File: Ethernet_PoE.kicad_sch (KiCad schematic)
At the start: 7 parts, among them J201 7499511002A, U201 AG5712-LPB

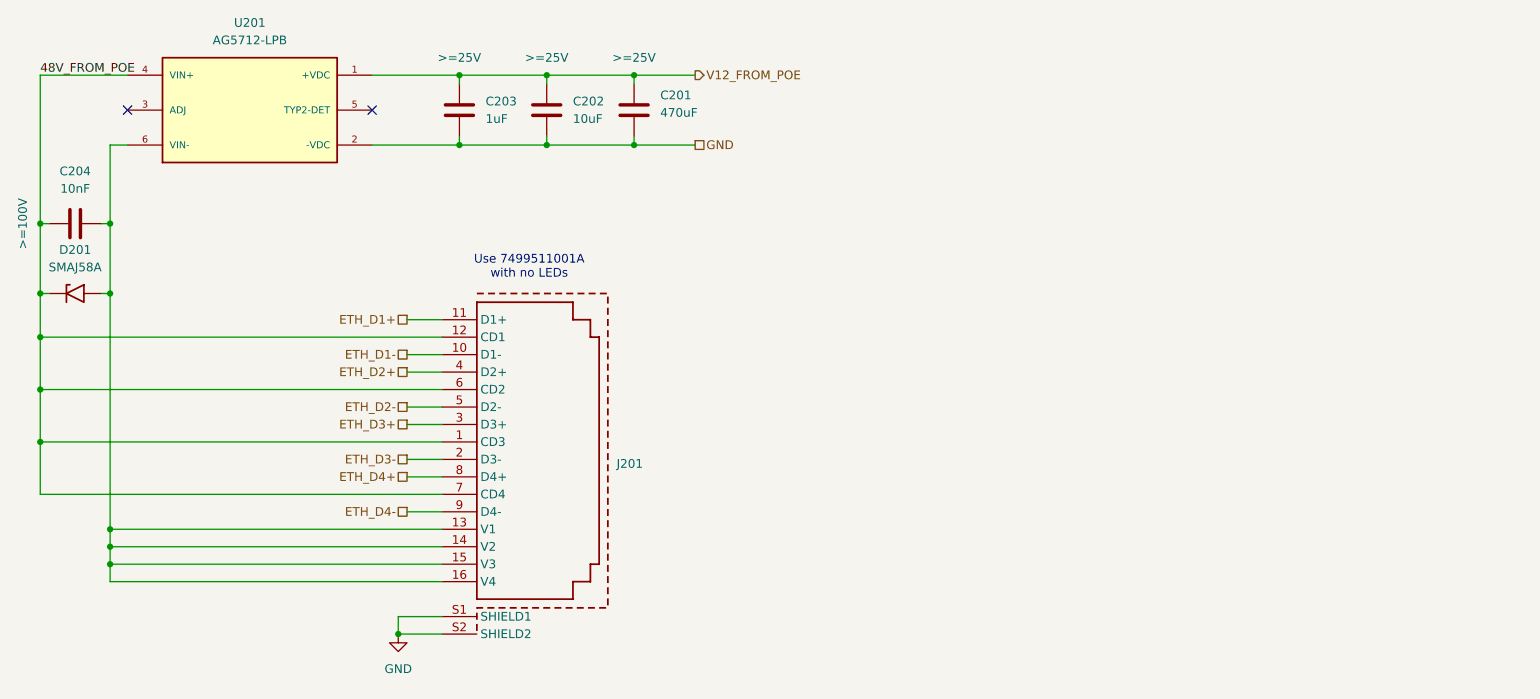
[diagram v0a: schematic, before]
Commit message: Update to fix power connection mistakes in both IWCD and HK configurations. For IWCD added bridge rectifier diodes needed for PoE, for HK updated to look at correct ref voltage for the 12V generation DC/DC, rotated the TVS to correct orientation and updated input diodes to be >=100V
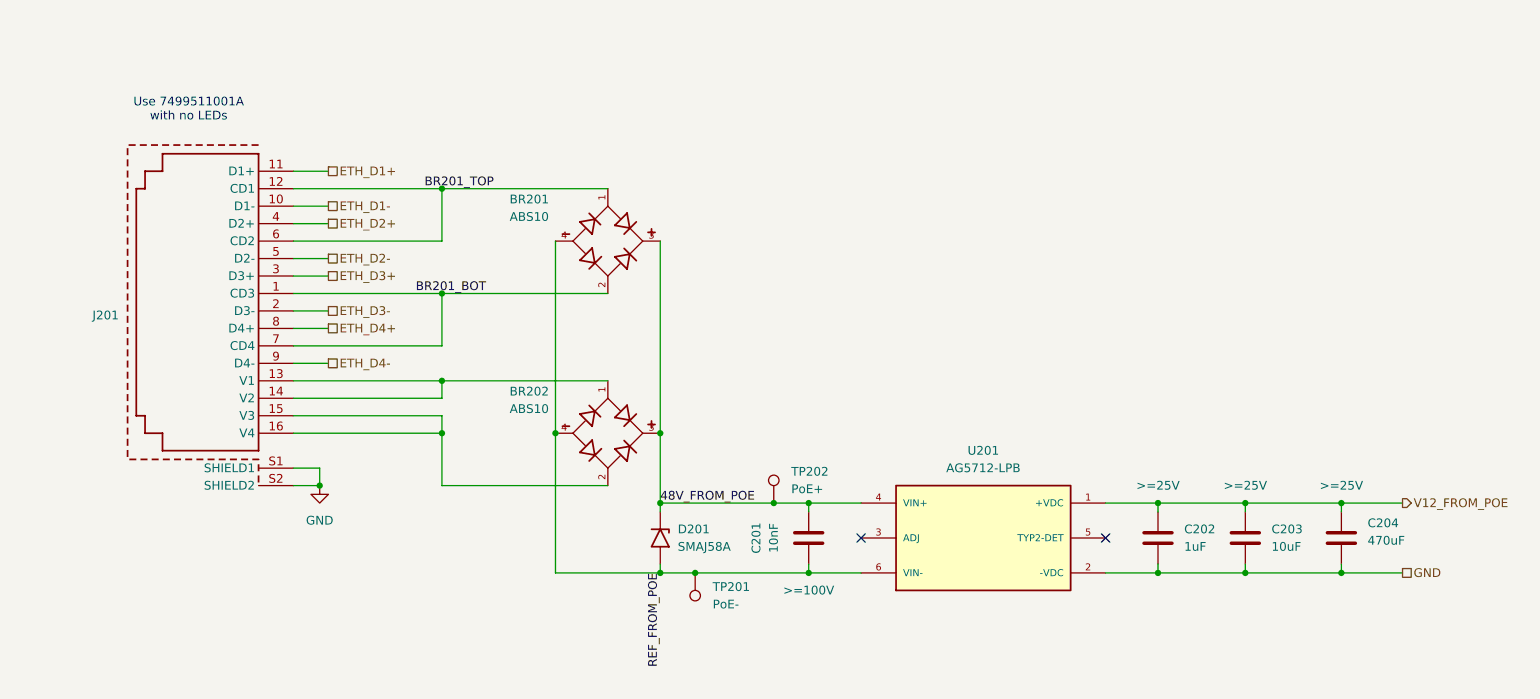
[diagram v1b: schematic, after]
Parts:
- added BR201, BR202: ABS10, ABS10:SOT200P640X160-4N, symbol ABS10:ABS10
- added TP201: PoE-, TestPoint:TestPoint_Pad_D1.5mm, symbol Connector:TestPoint
- added TP202: PoE+, TestPoint:TestPoint_Pad_D1.5mm, symbol Connector:TestPoint
- renumbered C204 to C201, C203 to C202, C202 to C203, C201 to C204
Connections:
- net 48V_FROM_POE: now also C201.2, BR201.3, BR202.3, TP202.1; no longer C201.1, J201.1 (CD3), J201.12 (CD1), J201.6 (CD2), J201.7 (CD4)
- new net: BR202.1, J201.13 (V1), J201.14 (V2)
- new net: BR202.2, J201.15 (V3), J201.16 (V4)
- new net BR201_BOT: BR201.2, J201.1 (CD3), J201.7 (CD4)
- new net BR201_TOP: BR201.1, J201.12 (CD1), J201.6 (CD2)
- new net REF_FROM_POE: BR201.4, BR202.4, C201.1, D201.2 (A2), TP201.1, U201.6 (VIN-)
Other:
- moved on the sheet: C201, C202, C203, C204, D201, J201, U201
